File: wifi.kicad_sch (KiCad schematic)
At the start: 6 parts, among them J6 WIFI_OFF, U9 ESP32-WROVER-E

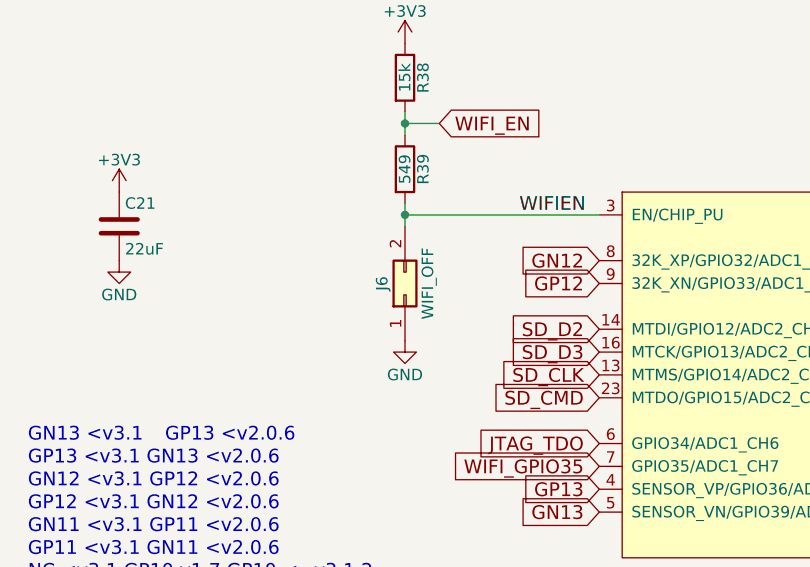
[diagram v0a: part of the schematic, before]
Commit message: Remove 'Leave Empty' in favor of using attributes
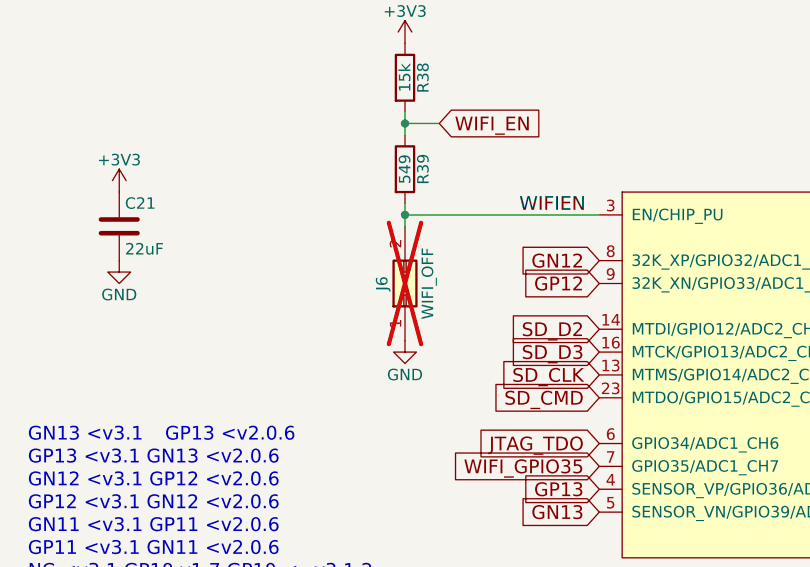
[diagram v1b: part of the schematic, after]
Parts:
- J6: Note Leave empty -> (none); now not fitted
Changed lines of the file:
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@@
 		(in_bom no)
 		(on_board yes)
-		(in_pos_files yes)
-		(dnp no)
+		(in_pos_files no)
+		(dnp yes)
 		(property "Reference" "J6"
 			(at 119.38 66.04 0)
@@
 			)
 		)
-		(property "Note" "Leave empty"
+		(property "Note" ""
 			(at 121.92 67.31 0)
 			(hide yes)

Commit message: update parts for 22uf/1uf. Update footprint for RP* items
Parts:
- C21: Digikey 1276-2413-1-ND -> 311-1900-1-ND; LCSC C29277 -> (none); MPN CC0805ZKY5V5BB226 -> 603-CC805MKX5R6BB226; MPN2 (none) -> CC0805ZKY5V5BB226
- U9: Digikey (none) -> 1965-ESP32-WROVER-E-N16R8CT-ND; MPN (none) -> 356-ESP32WRVE22864PC

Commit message: interim esp32 change
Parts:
- added C21: 22uF, Capacitor_SMD:C_0805_2012Metric, symbol Device:C
- added J6: WIFI_OFF, Connector_PinHeader_2.54mm:PinHeader_1x02_P2.54mm_Vertical, symbol Connector_Generic:Conn_02x01
- added R38: 15k, Resistor_SMD:R_0603_1608Metric, symbol Device:R
- added R39: 549, Resistor_SMD:R_0603_1608Metric, symbol Device:R
- added U9: ESP32-S3-WROOM-1, PCM_Espressif:ESP32-S3-WROOM-1, symbol esp32:ESP32-S3-WROOM-1
- C121: renamed from C21; now not fitted; now left out of the parts list
- R138: renamed from R38; now not fitted; now left out of the parts list
- R139: renamed from R39; now not fitted; now left out of the parts list
- U109: renamed from U9; now not fitted; now left out of the parts list
- renumbered J6 to J9
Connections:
- net +3V3: now also C21.1, R38.1, U9.2 (3V3)
- net GND: now also C21.2, J6.1 (Pin_1), U9.1 (GND), U9.40 (GND), U9.41 (GND)
- net JTAG_TCK: now also U9.10 (GPIO17/U1TXD/ADC2_CH6)
- net JTAG_TDI: now also U9.23 (GPIO21)
- net JTAG_TDO: now also U9.11 (GPIO18/U1RXD/ADC2_CH7/CLK_OUT3)
- net JTAG_TMS: now also U9.26 (GPIO45)
- net SD_CLK: now also U9.39 (GPIO1/TOUCH1/ADC1_CH0)
- net SD_CMD: now also U9.38 (GPIO2/TOUCH2/ADC1_CH1)
- net SD_D0: now also U9.4 (GPIO4/TOUCH4/ADC1_CH3)
- net SD_D1: now also U9.5 (GPIO5/TOUCH5/ADC1_CH4)
- net SD_D2: now also U9.6 (GPIO6/TOUCH6/ADC1_CH5)
- net SD_D3: now also U9.7 (GPIO7/TOUCH7/ADC1_CH6)
- net WIFIEN: now also J6.2 (Pin_2), R39.2, U9.3 (EN)
- net WIFI_EN: now also R38.2, R39.1
- net WIFI_GPIO0: now also U9.27 (GPIO0/BOOT)
- net WIFI_GPIO35: now also U9.28 (SPIIO6/GPIO35/FSPID/SUBSPID)
- net WIFI_RXD: now also U9.36 (U0RXD/GPIO44/CLK_OUT2)
- net WIFI_TXD: now also U9.37 (U0TXD/GPIO43/CLK_OUT1)
- new net WIFI_GPIO10: U9.18 (GPIO10/TOUCH10/ADC1_CH9/FSPICS0/FSPIIO4/SUBSPICS0)
- new net WIFI_GPIO11: U9.19 (GPIO11/TOUCH11/ADC2_CH0/FSPID/FSPIIO5/SUBSPID)
- new net WIFI_GPIO12: U9.20 (GPIO12/TOUCH12/ADC2_CH1/FSPICLK/FSPIIO6/SUBSPICLK)
- new net WIFI_GPIO13: U9.21 (GPIO13/TOUCH13/ADC2_CH2/FSPIQ/FSPIIO7/SUBSPIQ)
- new net WIFI_GPIO14: U9.22 (GPIO14/TOUCH14/ADC2_CH3/FSPIWP/FSPIDQS/SUBSPIWP)
- new net WIFI_GPIO15_XTAL_D+: U9.8 (GPIO15/U0RTS/ADC2_CH4/XTAL_32K_P)
- new net WIFI_GPIO16_XTAL_D-: U9.9 (GPIO16/U0CTS/ADC2_CH5/XTAL_32K_N)
- new net WIFI_GPIO3: U9.15 (GPIO3/TOUCH3/ADC1_CH2)
- new net WIFI_GPIO36: U9.29 (SPIIO7/GPIO36/FSPICLK/SUBSPICLK)
- new net WIFI_GPIO37: U9.30 (SPIDQS/GPIO37/FSPIQ/SUBSPIQ)
- new net WIFI_GPIO38: U9.31 (GPIO38/FSPIWP/SUBSPIWP)
- new net WIFI_GPIO39: U9.32 (MTCK/GPIO39/CLK_OUT3/SUBSPICS1)
- new net WIFI_GPIO40: U9.33 (MTDO/GPIO40/CLK_OUT2)
- new net WIFI_GPIO41: U9.34 (MTDI/GPIO41/CLK_OUT1)
- new net WIFI_GPIO42: U9.35 (MTMS/GPIO42)
- new net WIFI_GPIO46: U9.16 (GPIO46)
- new net WIFI_GPIO47_1V8: U9.24 (GPIO47/SPICLK_P/SUBSPICLK_P_DIFF)
- new net WIFI_GPIO48_1V8: U9.25 (GPIO48/SPICLK_N/SUBSPICLK_N_DIFF)
- new net WIFI_GPIO8: U9.12 (GPIO8/TOUCH8/ADC1_CH7/SUBSPICS1)
- new net WIFI_GPIO9: U9.17 (GPIO9/TOUCH9/ADC1_CH8/FSPIHD/SUBSPIHD)
- new net WIFI_USB_D+: U9.14 (GPIO20/U1CTS/ADC2_CH9/CLK_OUT1/USB_D+)
- new net WIFI_USB_D-: U9.13 (GPIO19/U1RTS/ADC2_CH8/CLK_OUT2/USB_D-)
- no-connect marks 0 -> 5
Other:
- note added: "GPIO{35,36,37} in use by ESP32 for PSRAM addressing!"
- note added: "JTAG netlists should be placed on general GPIO) TDO - I TDI - I/O TCK - I/O TMS - I/O"
- note added: "Strapping Pins: GPIO{2,3,45,46} WIFIEN no longer manipulates strapping - but it still does impact devices on-off. GPIO 0/46 now control boot behavior. replace EN for 46 in FPGA imaage"
- note removed: "GN10 v1.7"
- note removed: "GN11 <v3.1 GP11 <v2.0.6"
- note removed: "GN12 <v3.1 GP12 <v2.0.6"
- note removed: "GN13 <v3.1"
- note removed: "GP11 <v3.1 GN11 <v2.0.6"
- note removed: "GP12 <v3.1 GN12 <v2.0.6"
- note removed: "GP13 <v2.0.6"
- note removed: "GP13 <v3.1 GN13 <v2.0.6"
- note removed: "GP9 v1.7"
- note removed: "GPIO12 probably should be held low at reset or disconnected other option is to burn flash voltage efuse for 3.3V operation for GPIO2 and GPIO12 bootstrapping considerations, read https://github.com/espressif/esp-idf/tree/master/examples/storage/sd_card"
- note removed: "NC <v3.1 GP10 v1.7 GP10 <=v3.1.2"
- note removed: "SD card connected according to Arduino->Examples->ESP32->SD_MMC_Test https://github.com/espressif/esp-idf/blob/ master/examples/storage/sd_card/README.md"
- moved on the sheet: J9, R56

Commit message: reposition flash to bottom. route esp32-s3. fix drc issues
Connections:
- net WIFI_GPIO11 is gone; now on net GN13: U9.19 (GPIO11/TOUCH11/ADC2_CH0/FSPID/FSPIIO5/SUBSPID)
- net WIFI_GPIO12 is gone; now on net GP13: U9.20 (GPIO12/TOUCH12/ADC2_CH1/FSPICLK/FSPIIO6/SUBSPICLK)
- net WIFI_GPIO13 is gone; now on net GN12: U9.21 (GPIO13/TOUCH13/ADC2_CH2/FSPIQ/FSPIIO7/SUBSPIQ)
- net WIFI_GPIO14 is gone; now on net GP12: U9.22 (GPIO14/TOUCH14/ADC2_CH3/FSPIWP/FSPIDQS/SUBSPIWP)
- net JTAG_TCK: now also U9.4 (GPIO4/TOUCH4/ADC1_CH3); no longer U9.10 (GPIO17/U1TXD/ADC2_CH6)
- net JTAG_TDI: now also U9.6 (GPIO6/TOUCH6/ADC1_CH5); no longer U9.23 (GPIO21)
- net JTAG_TDO: now also U9.5 (GPIO5/TOUCH5/ADC1_CH4); no longer U9.11 (GPIO18/U1RXD/ADC2_CH7/CLK_OUT3)
- net JTAG_TMS: now also U9.7 (GPIO7/TOUCH7/ADC1_CH6); no longer U9.26 (GPIO45)
- net SD_D0: now also U9.10 (GPIO17/U1TXD/ADC2_CH6); no longer U9.4 (GPIO4/TOUCH4/ADC1_CH3)
- net SD_D1: now also U9.11 (GPIO18/U1RXD/ADC2_CH7/CLK_OUT3); no longer U9.5 (GPIO5/TOUCH5/ADC1_CH4)
- net SD_D2: now also U9.23 (GPIO21); no longer U9.6 (GPIO6/TOUCH6/ADC1_CH5)
- net SD_D3: now also U9.26 (GPIO45); no longer U9.7 (GPIO7/TOUCH7/ADC1_CH6)
- net WIFI_GPIO35: no longer U109.7 (GPIO35/ADC1_CH7)
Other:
- note added: "New Pins: - WIFI_GPIO15_XTAL_D+/- - WIFI_GPIO{39,40,41,42} - ESP32's JTAG - WIFI_GPIO{3,8,9,10,11,12,13,14,38,46} - WIFI_USB_D+/- Newly unconnected - WIFI_GPIO35 Newly removed - WIFI_GPIO{19,21,22,25,26,27}"
- note removed: "GPIO{35,36,37} in use by ESP32 for PSRAM addressing!"
- note removed: "JTAG netlists should be placed on general GPIO) TDO - I TDI - I/O TCK - I/O TMS - I/O"
- note removed: "WROVER GPIO16,17 used internally for PSRAM"
- note removed: "pin27 - NC >=v3.1.2"
- note removed: "pin28 - NC v1.7, >=v3.1.2"

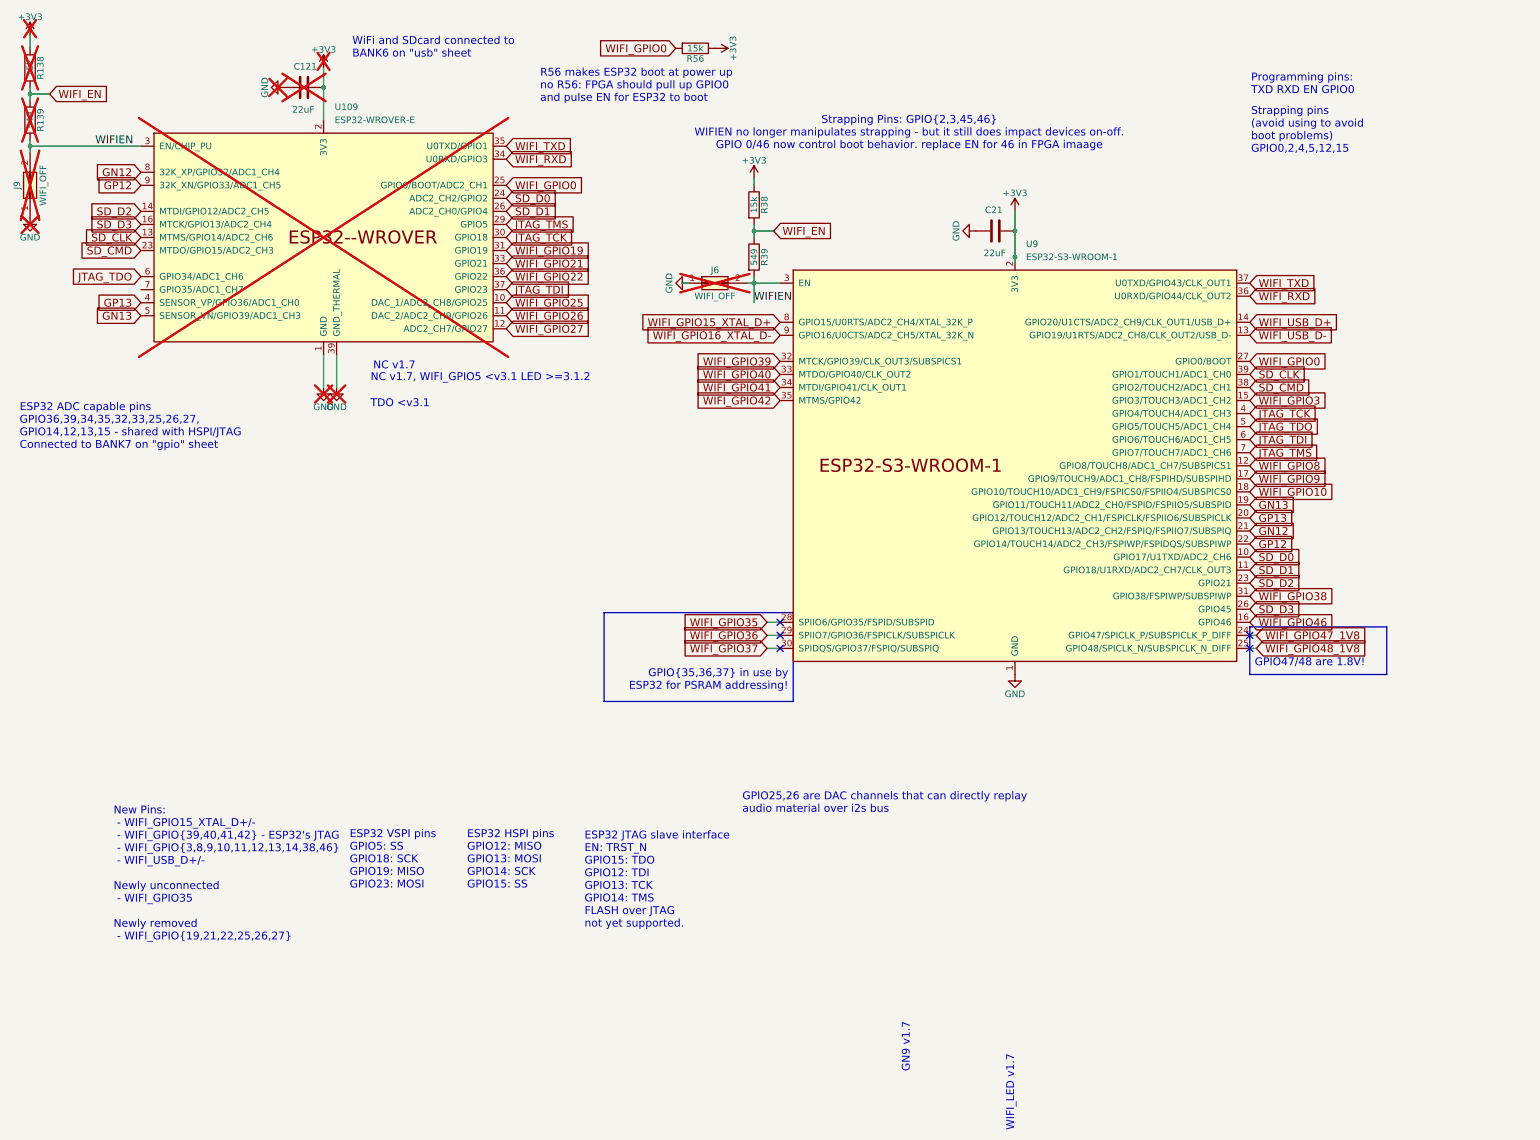
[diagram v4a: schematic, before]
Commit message: remove legacy esp32 from schematic
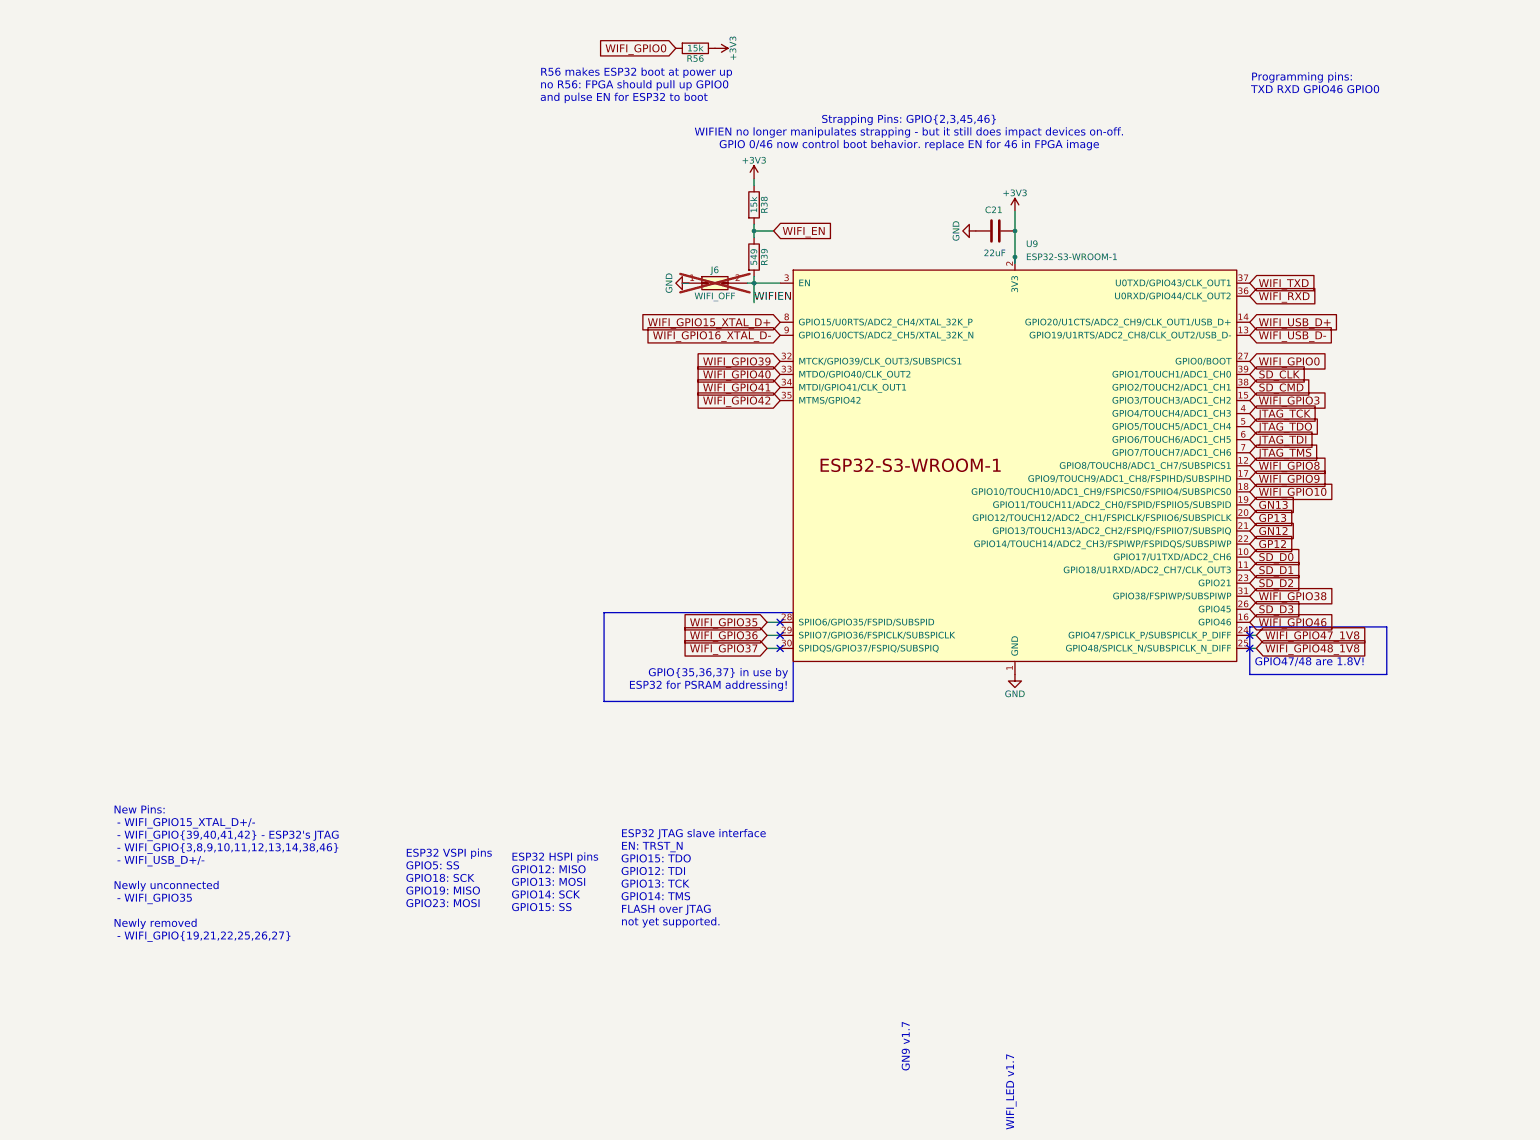
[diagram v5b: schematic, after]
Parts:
- removed C121: 22uF, Capacitor_SMD:C_0805_2012Metric, symbol Device:C
- removed J9: WIFI_OFF, Connector_PinHeader_2.54mm:PinHeader_1x02_P2.54mm_Vertical, symbol Connector_Generic:Conn_02x01
- removed R138: 15k, Resistor_SMD:R_0603_1608Metric, symbol Device:R
- removed R139: 549, Resistor_SMD:R_0603_1608Metric, symbol Device:R
- removed U109: ESP32-WROVER-E, PCM_Espressif:ESP32-WROVER-E, symbol PCM_Espressif:ESP32-WROVER-E
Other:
- note added: "Programming pins: TXD RXD GPIO46 GPIO0"
- note added: "Strapping Pins: GPIO{2,3,45,46} WIFIEN no longer manipulates strapping - but it still does impact devices on-off. GPIO 0/46 now control boot behavior. replace EN for 46 in FPGA image"
- note removed: "ESP32 ADC capable pins GPIO36,39,34,35,32,33,25,26,27, GPIO14,12,13,15 - shared with HSPI/JTAG Connected to BANK7 on "gpio" sheet"
- note removed: "GPIO25,26 are DAC channels that can directly replay audio material over i2s bus"
- note removed: "NC v1.7"
- note removed: "NC v1.7, WIFI_GPIO5 <v3.1 LED >=3.1.2"
- note removed: "Programming pins: TXD RXD EN GPIO0"
- note removed: "Strapping Pins: GPIO{2,3,45,46} WIFIEN no longer manipulates strapping - but it still does impact devices on-off. GPIO 0/46 now control boot behavior. replace EN for 46 in FPGA imaage"
- note removed: "Strapping pins (avoid using to avoid boot problems) GPIO0,2,4,5,12,15"
- note removed: "TDO <v3.1"
- note removed: "WiFi and SDcard connected to BANK6 on "usb" sheet"

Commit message: in progress, placement happend -- working on wiring
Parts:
- removed J6: WIFI_OFF, Connector_PinHeader_2.54mm:PinHeader_1x02_P2.54mm_Vertical, symbol Connector_Generic:Conn_02x01
- added RP7: 0, Resistor_SMD:R_0805_2012Metric_Pad1.20x1.40mm_HandSolder, symbol Device:Jumper_NC_Small
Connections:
- net GND: now also RP7.1
- net WIFIEN: now also RP7.2
